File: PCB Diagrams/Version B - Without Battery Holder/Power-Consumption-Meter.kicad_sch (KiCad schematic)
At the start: 35 parts, among them J1 Jack_DC, J10 01x02, J11 01x02, J12 01x02, J13 01x02, J2 01x02, J3 01x02, J4 USB_A, J5 Jack_DC, J6 Jack_DC, J7 USB_B_Mini, J8 USB_B_Micro, J9 01x04, SW1 SW_SPDT, SW2 SW_Push, U1 INA219_Module, U2 Display_5641BS

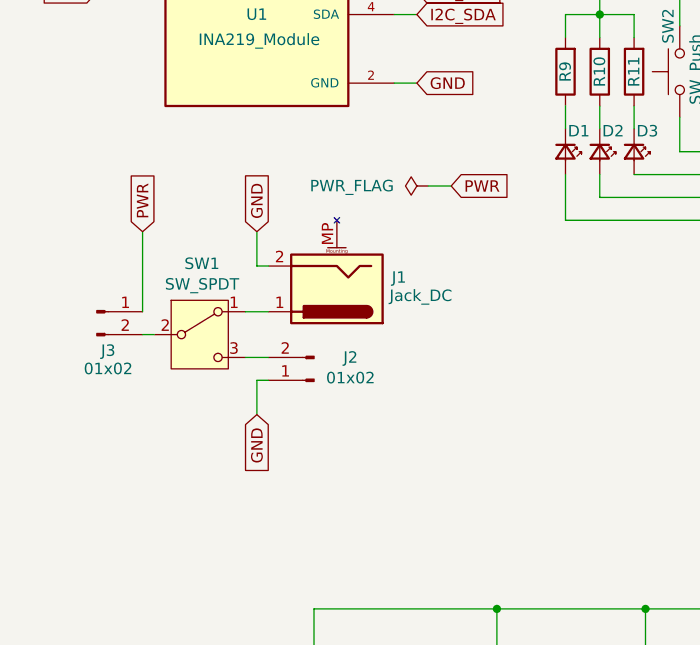
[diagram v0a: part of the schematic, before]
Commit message: update PCB connectors
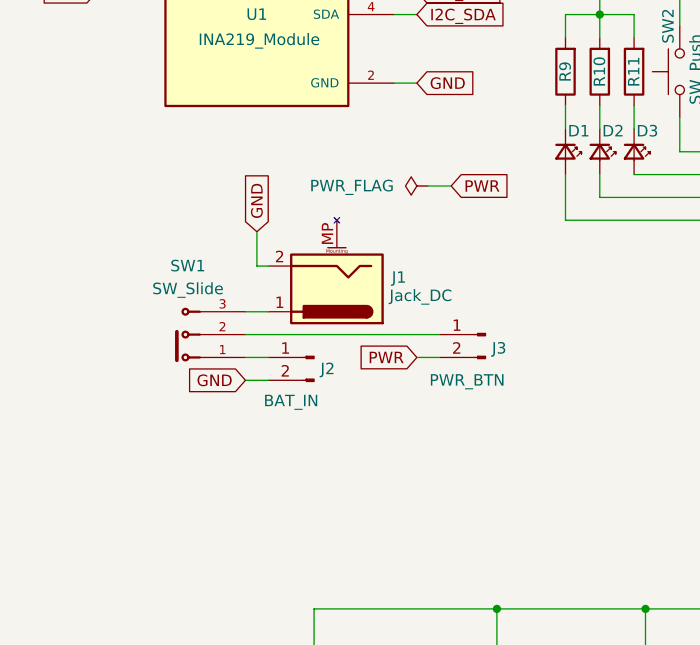
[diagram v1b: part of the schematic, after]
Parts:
- removed SW1: SW_SPDT, Button_Switch_THT:SW_Slide_SPDT_Straight_CK_OS102011MS2Q, symbol Switch:SW_SPDT
- added SW1: SW_Slide, Custom:Switch_Slide_SPDT_Straight_TE_1825159_1, symbol Custom:Switch_Slide_SPDT_Straight_TE_1825159_1
- J10, J11, J12, J13: footprint Connector_PinSocket_2.54mm:PinSocket_1x02_P2.54mm_Vertical -> Connector_JST:JST_EH_B2B-EH-A_1x02_P2.50mm_Vertical
- J2: value 01x02 -> BAT_IN
- J3: value 01x02 -> PWR_BTN
- J9: footprint Connector_PinSocket_2.54mm:PinSocket_1x04_P2.54mm_Vertical -> Connector_JST:JST_EH_B4B-EH-A_1x04_P2.50mm_Vertical
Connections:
- net GND: now also J2.2 (Pin_2); no longer J2.1 (Pin_1)
- net PWR: now also J3.2 (Pin_2); no longer J3.1 (Pin_1)
- net at J1.1: now also SW1.3
- new net: J2.1 (Pin_1), SW1.1
- new net: J3.1 (Pin_1), SW1.2
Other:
- moved on the sheet: J2, J3
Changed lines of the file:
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@@
 	(wire
 		(pts
-			(xy 52.07 81.28) (xy 50.8 81.28)
-		)
-		(stroke
-			(width 0)
-			(type default)
-		)
-	)
-	(wire
-		(pts
 			(xy 90.17 111.76) (xy 90.17 127)
 		)
@@
 	(wire
 		(pts
+			(xy 62.23 81.28) (xy 83.82 81.28)
+		)
+		(stroke
+			(width 0)
+			(type default)
+		)
+	)
+	(wire
+		(pts
 			(xy 62.23 83.82) (xy 64.77 83.82)
 		)
@@
 	(wire
 		(pts
+			(xy 81.28 83.82) (xy 83.82 83.82)
+		)
+		(stroke
+			(width 0)
+			(type default)
+		)
+	)
+	(wire
+		(pts
 			(xy 175.26 55.88) (xy 177.8 55.88)
 		)
@@
 	(wire
 		(pts
-			(xy 63.5 90.17) (xy 63.5 86.36)
-		)
-		(stroke
-			(width 0)
-			(type default)
-		)
-	)
-	(wire
-		(pts
-			(xy 50.8 69.85) (xy 50.8 78.74)
-		)
-		(stroke
-			(width 0)
-			(type default)
-		)
-	)
-	(wire
-		(pts
 			(xy 198.12 111.76) (xy 198.12 128.27)
 		)
@@
 	(wire
 		(pts
-			(xy 63.5 86.36) (xy 64.77 86.36)
+			(xy 62.23 86.36) (xy 64.77 86.36)
 		)
 		(stroke
@@
 		)
 	)
-	(global_label "PWR"
-		(shape input)
-		(at 50.8 69.85 90)
-		(fields_autoplaced yes)
-		(effects
-			(font
-				(size 1.27 1.27)
-			)
-			(justify left)
-		)
-		(property "Intersheetrefs" "${INTERSHEET_REFS}"
-			(at 50.8 62.8734 90)
-			(effects
-				(font
-					(size 1.27 1.27)
-				)
-				(justify left)
-				(hide yes)
-			)
-		)
-	)
 	(global_label "SEG_P"
 		(shape input)
@@
 		)
 	)
+	(global_label "PWR"
+		(shape input)
+		(at 81.28 83.82 180)
+		(fields_autoplaced yes)
+		(effects
+			(font
+				(size 1.27 1.27)
+			)
+			(justify right)
+		)
+		(property "Intersheetrefs" "${INTERSHEET_REFS}"
+			(at 74.3034 83.82 0)
+			(effects
+				(font
+					(size 1.27 1.27)
+				)
+				(justify right)
+				(hide yes)
+			)
+		)
+	)
 	(global_label "SEG_D"
 		(shape input)
@@
 	(global_label "GND"
 		(shape input)
-		(at 63.5 90.17 270)
+		(at 62.23 86.36 180)
 		(fields_autoplaced yes)
 		(effects
@@
 		)
 		(property "Intersheetrefs" "${INTERSHEET_REFS}"
-			(at 63.5 97.0257 90)
+			(at 55.3743 86.36 0)
 			(effects
 				(font
@@
 	)
 	(symbol
+		(lib_id "Custom:Switch_Slide_SPDT_Straight_TE_1825159_1")
+		(at 54.61 81.28 180)
+		(unit 1)
+		(exclude_from_sim no)
+		(in_bom yes)
+		(on_board yes)
+		(dnp no)
+		(fields_autoplaced yes)
+		(property "Reference" "SW1"
+			(at 55.8419 73.66 0)
+			(effects
+				(font
+					(size 1.27 1.27)
+				)
+			)
+		)
+		(property "Value" "SW_Slide"
+			(at 55.8419 76.2 0)
+			(effects
+				(font
+					(size 1.27 1.27)
+				)
+			)
+		)
+		(property "Footprint" "Custom:Switch_Slide_SPDT_Straight_TE_1825159_1"
+			(at 59.69 66.294 0)
+			(effects
+				(font
+					(size 1.27 1.27)
+				)
+				(justify bottom)
+				(hide yes)
+			)
+		)
+		(property "Datasheet" ""
+			(at 54.61 81.28 0)
+			(effects
+				(font
+					(size 1.27 1.27)
+				)
+				(hide yes)
+			)
+		)
+		(property "Description" "SWITCH SLIDE SPDT 300MA 125V"
+			(at 57.658 69.85 0)
+			(effects
+				(font
+					(size 1.27 1.27)
+				)
+				(hide yes)
+			)
+		)
+		(property "MF" "TE Connectivity"
+			(at 65.532 63.5 0)
+			(effects
+				(font
+					(size 1.27 1.27)
+				)
+				(justify bottom)
+				(hide yes)
+			)
+		)
+		(property "MP" "1825159-1"
+			(at 50.038 63.754 0)
+			(effects
+				(font
+					(size 1.27 1.27)
+				)
+				(justify bottom)
+				(hide yes)
+			)
+		)
+		(pin "2"
+		)
+		(pin "1"
+		)
+		(pin "3"
+		)
+		(instances
+			(project ""
+				(path "/04a21a1e-c762-45c9-8522-5107851ca11f"
+					(reference "SW1")
+					(unit 1)
+				)
+			)
+		)
+	)
+	(symbol
 		(lib_id "Connector:Conn_01x02_Pin")
-		(at 45.72 78.74 0)
+		(at 88.9 81.28 0)
+		(mirror y)
 		(unit 1)
 		(exclude_from_sim no)
@@
 		(dnp no)
 		(property "Reference" "J3"
-			(at 46.99 83.058 0)
+			(at 90.424 82.804 0)
 			(effects
 				(font
@@
 			)
 		)
-		(property "Value" "01x02"
-			(at 46.99 85.09 0)
+		(property "Value" "PWR_BTN"
+			(at 86.868 86.36 0)
 			(effects
 				(font
@@
 		)
 		(property "Footprint" "Connector_PinHeader_2.54mm:PinHeader_1x02_P2.54mm_Vertical"
-			(at 45.72 78.74 0)
+			(at 88.9 81.28 0)
 			(effects
 				(font
@@
 		)
 		(property "Datasheet" "~"
-			(at 45.72 78.74 0)
+			(at 88.9 81.28 0)
 			(effects
 				(font
@@
 		)
 		(property "Description" "Generic connector, single row, 01x02, script generated"
-			(at 45.72 78.74 0)
+			(at 88.9 81.28 0)
 			(effects
 				(font
@@
 			)
 		)
-		(property "Footprint" "Connector_PinSocket_2.54mm:PinSocket_1x02_P2.54mm_Vertical"
+		(property "Footprint" "Connector_JST:JST_EH_B2B-EH-A_1x02_P2.50mm_Vertical"
 			(at 203.2 130.81 0)
 			(effects
@@
 			)
 		)
-		(property "Footprint" "Connector_PinSocket_2.54mm:PinSocket_1x02_P2.54mm_Vertical"
+		(property "Footprint" "Connector_JST:JST_EH_B2B-EH-A_1x02_P2.50mm_Vertical"
 			(at 217.17 130.81 0)
 			(effects
@@
 	)
 	(symbol
-		(lib_id "Switch:SW_SPDT")
-		(at 57.15 81.28 0)
-		(unit 1)
-		(exclude_from_sim no)
-		(in_bom yes)
-		(on_board yes)
-		(dnp no)
-		(property "Reference" "SW1"
-			(at 57.404 73.406 0)
-			(effects
-				(font
-					(size 1.27 1.27)
-				)
-			)
-		)
-		(property "Value" "SW_SPDT"
-			(at 57.404 75.692 0)
-			(effects
-				(font
-					(size 1.27 1.27)
-				)
-			)
-		)
-		(property "Footprint" "Button_Switch_THT:SW_Slide_SPDT_Straight_CK_OS102011MS2Q"
-			(at 57.15 81.28 0)
-			(effects
-				(font
-					(size 1.27 1.27)
-				)
-				(hide yes)
-			)
-		)
-		(property "Datasheet" "~"
-			(at 57.15 88.9 0)
-			(effects
-				(font
-					(size 1.27 1.27)
-				)
-				(hide yes)
-			)
-		)
-		(property "Description" "Switch, single pole double throw"
-			(at 57.15 81.28 0)
-			(effects
-				(font
-					(size 1.27 1.27)
-				)
-				(hide yes)
-			)
-		)
-		(pin "3"
-		)
-		(pin "1"
-		)
-		(pin "2"
-		)
-		(instances
-			(project ""
-				(path "/04a21a1e-c762-45c9-8522-5107851ca11f"
-					(reference "SW1")
-					(unit 1)
-				)
-			)
-		)
-	)
-	(symbol
 		(lib_id "Device:R")
 		(at 97.79 52.07 180)
@@
 	(symbol
 		(lib_id "Connector:Conn_01x02_Pin")
-		(at 69.85 86.36 180)
+		(at 69.85 83.82 0)
+		(mirror y)
 		(unit 1)
 		(exclude_from_sim no)
@@
 		(dnp no)
 		(property "Reference" "J2"
-			(at 73.914 83.82 0)
+			(at 71.374 85.09 0)
 			(effects
 				(font
@@
 			)
 		)
-		(property "Value" "01x02"
-			(at 73.914 86.106 0)
+		(property "Value" "BAT_IN"
+			(at 67.31 88.646 0)
 			(effects
 				(font
@@
 		)
 		(property "Footprint" "Connector_PinHeader_2.54mm:PinHeader_1x02_P2.54mm_Vertical"
-			(at 69.85 86.36 0)
+			(at 69.85 83.82 0)
 			(effects
 				(font
@@
 		)
 		(property "Datasheet" "~"
-			(at 69.85 86.36 0)
+			(at 69.85 83.82 0)
 			(effects
 				(font
@@
 		)
 		(property "Description" "Generic connector, single row, 01x02, script generated"
-			(at 69.85 86.36 0)
+			(at 69.85 83.82 0)
 			(effects
 				(font
@@
 		)
 		(instances
-			(project ""
+			(project "Power-Consumption-Meter"
 				(path "/04a21a1e-c762-45c9-8522-5107851ca11f"
 					(reference "J2")
@@
 			)
 		)
-		(property "Footprint" "Connector_PinSocket_2.54mm:PinSocket_1x02_P2.54mm_Vertical"
+		(property "Footprint" "Connector_JST:JST_EH_B2B-EH-A_1x02_P2.50mm_Vertical"
 			(at 182.88 130.81 0)
 			(effects
@@
 			)
 		)
-		(property "Footprint" "Connector_PinSocket_2.54mm:PinSocket_1x02_P2.54mm_Vertical"
+		(property "Footprint" "Connector_JST:JST_EH_B2B-EH-A_1x02_P2.50mm_Vertical"
 			(at 193.04 130.81 0)
 			(effects
@@
 			)
 		)
-		(property "Footprint" "Connector_PinSocket_2.54mm:PinSocket_1x04_P2.54mm_Vertical"
+		(property "Footprint" "Connector_JST:JST_EH_B4B-EH-A_1x04_P2.50mm_Vertical"
 			(at 168.91 130.81 0)
 			(effects

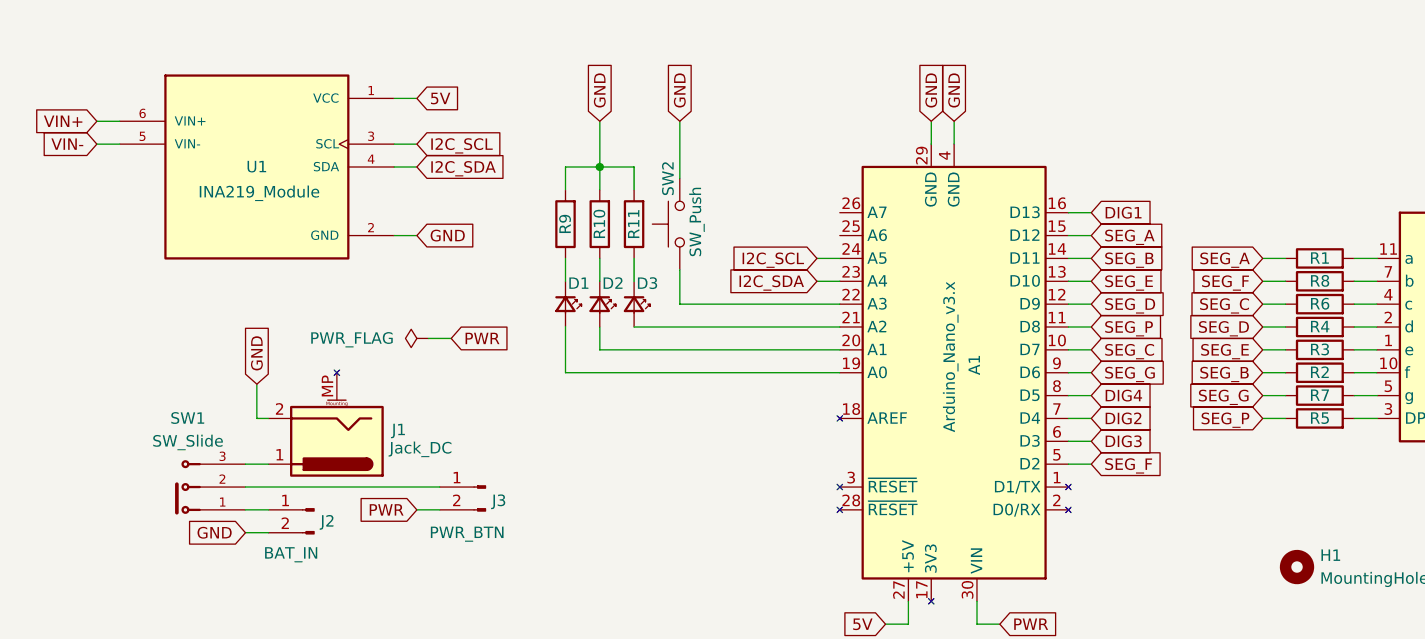
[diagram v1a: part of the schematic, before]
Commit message: Adding PCB building and assembly pictures
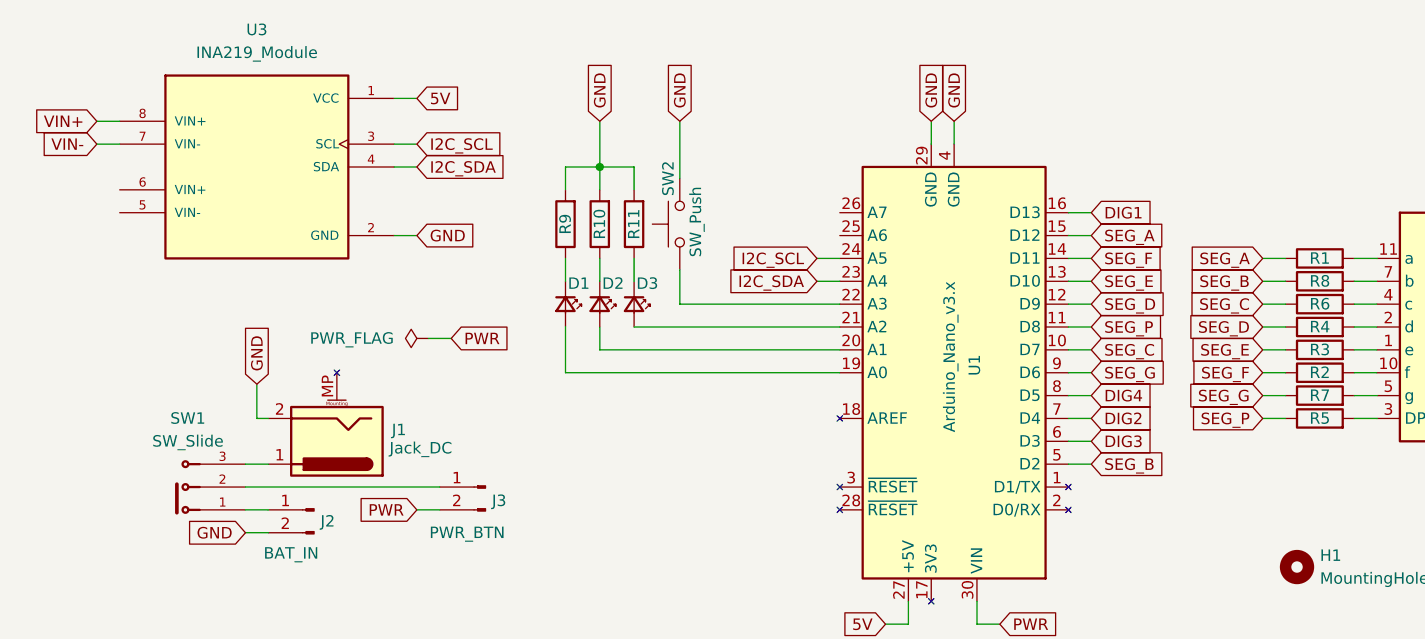
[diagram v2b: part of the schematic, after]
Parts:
- removed U1: INA219_Module, Custom:INA219_Module_Adafruit, symbol Custom:INA219_Module
- added U3: INA219_Module, Custom:INA219_Module_Generic, symbol Custom:INA219_Module_Adafruit
- renumbered A1 to U1
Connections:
- net 5V: now also U3.1 (VCC)
- net GND: now also U3.2 (GND)
- net I2C_SCL: now also U3.3 (SCL)
- net I2C_SDA: now also U3.4 (SDA)
- net SEG_B: now also R8.1, U1.5 (D2); no longer R2.1, U1.14 (D11)
- net SEG_F: now also R2.1, U1.14 (D11); no longer R8.1, U1.5 (D2)
- net VIN+: now also U3.8 (VIN+)
- net VIN-: now also U3.7 (VIN-)
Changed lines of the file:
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@@
 	(wire
 		(pts
-			(xy 45.72 40.64) (xy 48.26 40.64)
-		)
-		(stroke
-			(width 0)
-			(type default)
-		)
-	)
-	(wire
-		(pts
 			(xy 101.6 58.42) (xy 101.6 55.88)
 		)
@@
 	(wire
 		(pts
+			(xy 45.72 40.64) (xy 48.26 40.64)
+		)
+		(stroke
+			(width 0)
+			(type default)
+		)
+	)
+	(wire
+		(pts
 			(xy 187.96 55.88) (xy 185.42 55.88)
 		)
@@
 	(wire
 		(pts
-			(xy 97.79 45.72) (xy 97.79 48.26)
+			(xy 45.72 43.18) (xy 48.26 43.18)
 		)
 		(stroke
@@
 	(wire
 		(pts
-			(xy 187.96 111.76) (xy 187.96 128.27)
+			(xy 97.79 45.72) (xy 97.79 48.26)
 		)
 		(stroke
@@
 	(wire
 		(pts
-			(xy 90.17 132.08) (xy 90.17 147.32)
+			(xy 187.96 111.76) (xy 187.96 128.27)
 		)
 		(stroke
@@
 	(wire
 		(pts
-			(xy 101.6 45.72) (xy 105.41 45.72)
+			(xy 90.17 132.08) (xy 90.17 147.32)
 		)
 		(stroke
@@
 	(wire
 		(pts
-			(xy 143.51 93.98) (xy 143.51 96.52)
+			(xy 101.6 45.72) (xy 105.41 45.72)
 		)
 		(stroke
@@
 	(wire
 		(pts
-			(xy 101.6 66.04) (xy 101.6 63.5)
+			(xy 143.51 93.98) (xy 143.51 96.52)
 		)
 		(stroke
@@
 	(wire
 		(pts
-			(xy 45.72 43.18) (xy 48.26 43.18)
+			(xy 101.6 66.04) (xy 101.6 63.5)
 		)
 		(stroke
@@
 		)
 	)
-	(global_label "VIN+"
-		(shape input)
-		(at 45.72 40.64 180)
-		(fields_autoplaced yes)
-		(effects
-			(font
-				(size 1.27 1.27)
-			)
-			(justify right)
-		)
-		(property "Intersheetrefs" "${INTERSHEET_REFS}"
-			(at 38.1385 40.64 0)
-			(effects
-				(font
-					(size 1.27 1.27)
-				)
-				(justify right)
-				(hide yes)
-			)
-		)
-	)
-	(global_label "VIN-"
-		(shape input)
-		(at 45.72 43.18 180)
-		(fields_autoplaced yes)
-		(effects
-			(font
-				(size 1.27 1.27)
-			)
-			(justify right)
-		)
-		(property "Intersheetrefs" "${INTERSHEET_REFS}"
-			(at 38.1385 43.18 0)
-			(effects
-				(font
-					(size 1.27 1.27)
-				)
-				(justify right)
-				(hide yes)
-			)
-		)
-	)
 	(global_label "SEG_G"
 		(shape input)
@@
 		)
 	)
-	(global_label "SEG_B"
+	(global_label "SEG_F"
 		(shape input)
 		(at 156.21 55.88 0)
@@
 		)
 		(property "Intersheetrefs" "${INTERSHEET_REFS}"
-			(at 165.0613 55.88 0)
+			(at 164.8799 55.88 0)
 			(effects
 				(font
@@
 		)
 	)
-	(global_label "SEG_F"
+	(global_label "SEG_B"
 		(shape input)
 		(at 175.26 58.42 180)
@@
 		)
 		(property "Intersheetrefs" "${INTERSHEET_REFS}"
-			(at 166.5901 58.42 0)
+			(at 166.4087 58.42 0)
 			(effects
 				(font
@@
 		)
 	)
+	(global_label "VIN-"
+		(shape input)
+		(at 45.72 43.18 180)
+		(fields_autoplaced yes)
+		(effects
+			(font
+				(size 1.27 1.27)
+			)
+			(justify right)
+		)
+		(property "Intersheetrefs" "${INTERSHEET_REFS}"
+			(at 38.1385 43.18 0)
+			(effects
+				(font
+					(size 1.27 1.27)
+				)
+				(justify right)
+				(hide yes)
+			)
+		)
+	)
 	(global_label "GND"
 		(shape input)
@@
 		)
 	)
-	(global_label "SEG_B"
+	(global_label "SEG_F"
 		(shape input)
 		(at 175.26 68.58 180)
@@
 		)
 		(property "Intersheetrefs" "${INTERSHEET_REFS}"
-			(at 166.4087 68.58 0)
+			(at 166.5901 68.58 0)
 			(effects
 				(font
@@
 		)
 	)
-	(global_label "SEG_F"
+	(global_label "SEG_B"
 		(shape input)
 		(at 156.21 78.74 0)
@@
 		)
 		(property "Intersheetrefs" "${INTERSHEET_REFS}"
-			(at 164.8799 78.74 0)
+			(at 165.0613 78.74 0)
 			(effects
 				(font
@@
 		)
 	)
+	(global_label "VIN+"
+		(shape input)
+		(at 45.72 40.64 180)
+		(fields_autoplaced yes)
+		(effects
+			(font
+				(size 1.27 1.27)
+			)
+			(justify right)
+		)
+		(property "Intersheetrefs" "${INTERSHEET_REFS}"
+			(at 38.1385 40.64 0)
+			(effects
+				(font
+					(size 1.27 1.27)
+				)
+				(justify right)
+				(hide yes)
+			)
+		)
+	)
 	(global_label "SEG_C"
 		(shape input)
@@
 		(on_board yes)
 		(dnp no)
-		(property "Reference" "A1"
+		(property "Reference" "U1"
 			(at 143.256 66.548 90)
 			(effects
@@
 			(project ""
 				(path "/04a21a1e-c762-45c9-8522-5107851ca11f"
-					(reference "A1")
+					(reference "U1")
 					(unit 1)
 				)
@@
 	)
 	(symbol
-		(lib_id "Custom:INA219_Module")
-		(at 63.5 45.72 0)
-		(unit 1)
-		(exclude_from_sim no)
-		(in_bom yes)
-		(on_board yes)
-		(dnp no)
-		(property "Reference" "U1"
-			(at 63.5 45.72 0)
-			(effects
-				(font
-					(size 1.27 1.27)
-				)
-			)
-		)
-		(property "Value" "INA219_Module"
-			(at 63.754 48.514 0)
-			(effects
-				(font
-					(size 1.27 1.27)
-				)
-			)
-		)
-		(property "Footprint" "Custom:INA219_Module_Adafruit"
-			(at 18.796 66.802 0)
-			(effects
-				(font
-					(size 1.27 1.27)
-				)
-				(justify bottom)
-				(hide yes)
-			)
-		)
-		(property "Datasheet" ""
-			(at 63.5 45.72 0)
-			(effects
-				(font
-					(size 1.27 1.27)
-				)
-				(hide yes)
-			)
-		)
-		(property "Description" ""
-			(at 63.5 45.72 0)
-			(effects
-				(font
-					(size 1.27 1.27)
-				)
-				(hide yes)
-			)
-		)
-		(property "MP" "INA219"
-			(at 11.176 64.262 0)
-			(effects
-				(font
-					(size 1.27 1.27)
-				)
-				(justify bottom)
-				(hide yes)
-			)
-		)
-		(property "SNAPEDA_PN" "INA219 High Side DC Current Sensor Breakout - 26V ±3.2A Max - STEMMA QT"
-			(at 46.228 69.596 0)
-			(effects
-				(font
-					(size 1.27 1.27)
-				)
-				(justify bottom)
-				(hide yes)
-			)
-		)
-		(pin "4"
-		)
-		(pin "3"
-		)
-		(pin "5"
-		)
-		(pin "6"
-		)
-		(pin "1"
-		)
-		(pin "SH1"
-		)
-		(pin "2"
-		)
-		(instances
-			(project ""
-				(path "/04a21a1e-c762-45c9-8522-5107851ca11f"
-					(reference "U1")
-					(unit 1)
-				)
-			)
-		)
-	)
-	(symbol
 		(lib_id "Device:R")
 		(at 97.79 52.07 180)
@@
 					(unit 1)
 				)
+			)
+		)
+	)
+	(symbol
+		(lib_id "Custom:INA219_Module_Adafruit")
+		(at 63.5 45.72 0)
+		(unit 1)
+		(exclude_from_sim no)
+		(in_bom yes)
+		(on_board yes)
+		(dnp no)
+		(fields_autoplaced yes)
+		(property "Reference" "U3"
+			(at 63.5 30.48 0)
+			(effects
+				(font
+					(size 1.27 1.27)
+				)
+			)
+		)
+		(property "Value" "INA219_Module"
+			(at 63.5 33.02 0)
+			(effects
+				(font
+					(size 1.27 1.27)
+				)
+			)
+		)
+		(property "Footprint" "Custom:INA219_Module_Generic"
+			(at 44.196 68.834 0)
+			(effects
+				(font
+					(size 1.27 1.27)
+				)
+				(justify bottom)
+				(hide yes)
+			)
+		)
+		(property "Datasheet" ""
+			(at 63.5 45.72 0)
+			(effects
+				(font
+					(size 1.27 1.27)
+				)
+				(hide yes)
+			)
+		)
+		(property "Description" ""
+			(at 63.5 45.72 0)
+			(effects
+				(font
+					(size 1.27 1.27)
+				)
+				(hide yes)
+			)
+		)
+		(property "MP" "INA219"
+			(at 36.576 66.294 0)
+			(effects
+				(font
+					(size 1.27 1.27)
+				)
+				(justify bottom)
+				(hide yes)
+			)
+		)
+		(property "SNAPEDA_PN" "INA219 High Side DC Current Sensor Breakout - 26V ±3.2A Max - STEMMA QT"
+			(at 71.628 71.628 0)
+			(effects
+				(font
+					(size 1.27 1.27)
+				)
+				(justify bottom)
+				(hide yes)
+			)
+		)
+		(pin "6"
+		)
+		(pin "8"
+		)
+		(pin "1"
+		)
+		(pin "5"
+		)
+		(pin "3"
+		)
+		(pin "4"
+		)
+		(pin "2"
+		)
+		(pin "7"
+		)
+		(instances
+			(project ""
+				(path "/04a21a1e-c762-45c9-8522-5107851ca11f"
+					(reference "U3")
+					(unit 1)
+				)
